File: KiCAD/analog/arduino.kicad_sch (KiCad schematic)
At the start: 49 parts, among them J12 Screw_Terminal_01x04, J13 Screw_Terminal_01x03, J14 Screw_Terminal_01x05, J17 Conn_Coaxial_Small, J18 Conn_Coaxial_Small, J19 Conn_Coaxial_Small, J20 Screw_Terminal_01x04, J21 Screw_Terminal_01x02, J22 Screw_Terminal_01x04, J23 Conn_Coaxial_Small, J24 Conn_Coaxial_Small, J6 Screw_Terminal_01x02, J7 Screw_Terminal_01x02, J8 Screw_Terminal_01x02, J9 Screw_Terminal_01x02, Q4 2N7000, Q5 2N7000, Q6 2N7000, Q7 2N7000, U1 MCP1700x-330xxTO, U17 Adafruit_PCF8575_Breakout, U18 CD14538B, U3 MCP4728

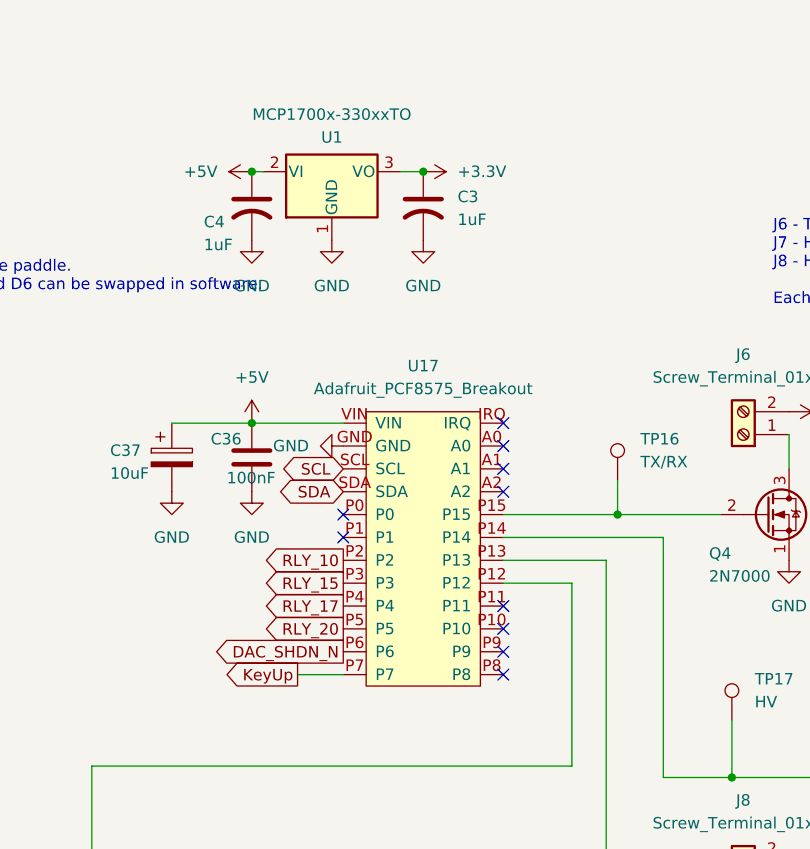
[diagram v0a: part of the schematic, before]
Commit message: KiCad revC: +28V doubler + 5V LDO added to analog/power, ERC clean
- Migrated LT1054 Figure 20 positive doubler from standalone power project
  into analog/power.kicad_sch for the +28V reed-relay rail
- Added LM2940CT-5.0 LDO stage for Metro / Si5351 +5V rail
- analog ERC: 4 messages, all classified as false positives (U9 pin 5
  tied to GND per Fig 20 topology, PCF_P5_SPARE intentionally unused,
  VIN pins now driven by added +5V rail)
- Added QRP Labs 10W PA / 5W PA reference PDFs + 2N7000 + lm2940c
  datasheets to Documentation/QRP_Examples/

Co-Authored-By: Claude Opus 4.7 <noreply@anthropic.com>
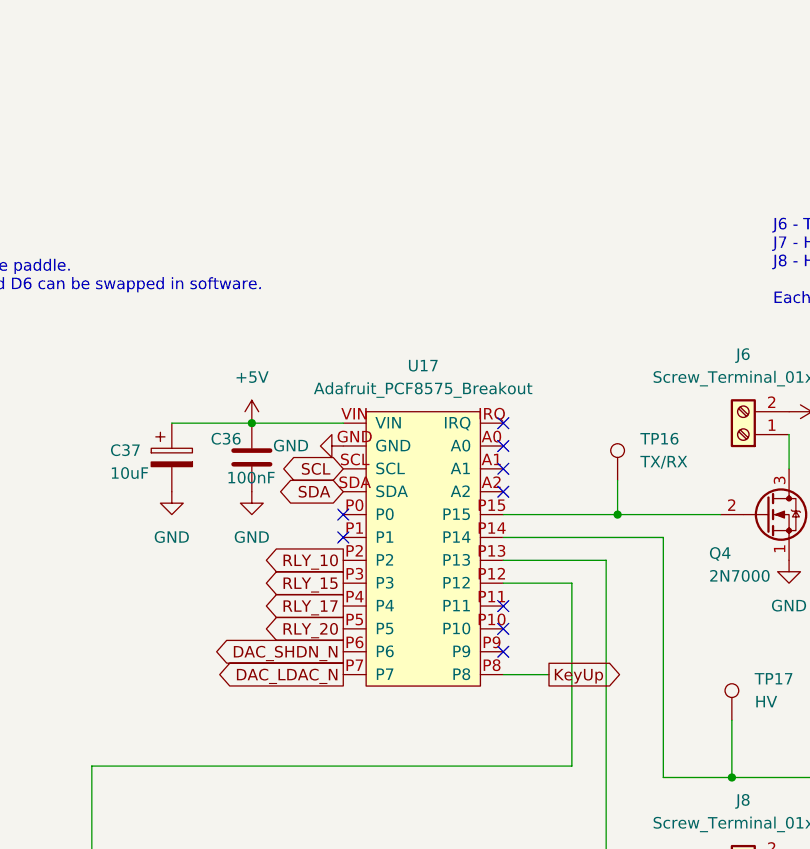
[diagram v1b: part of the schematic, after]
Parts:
- removed C3, C4: 1uF, Capacitor_THT:C_Rect_L7.2mm_W4.5mm_P5.00mm, symbol Device:C_US
- removed U1: MCP1700x-330xxTO, Package_TO_SOT_THT:TO-92_Inline_Wide, symbol Regulator_Linear:MCP1700x-330xxTO
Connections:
- net KeyUp: now also U17.P8; no longer U17.P7
- new net DAC_LDAC_N: U17.P7
- no-connect marks 18 -> 17

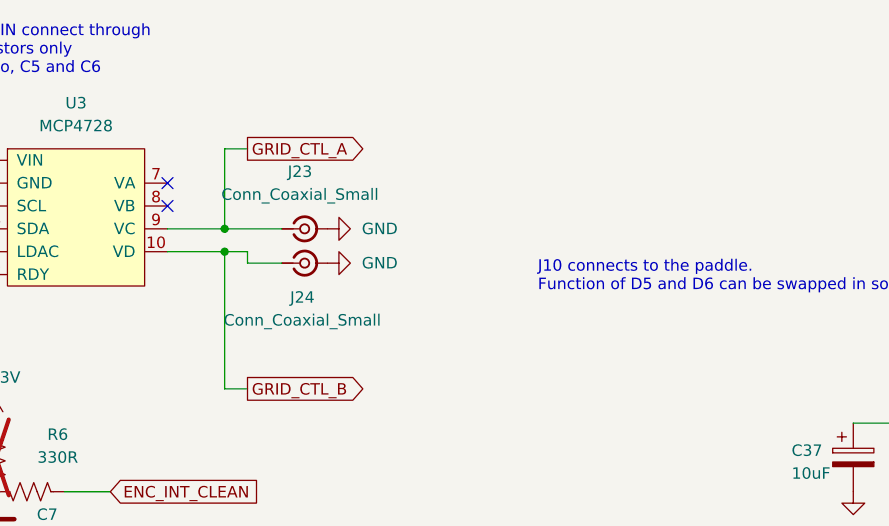
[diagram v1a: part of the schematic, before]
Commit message: KiCad revC: repurpose MCP4728 VA/VB as Bias_A/Bias_B for SS PA
Add Bias_A and Bias_B global labels off the MCP4728 (U? on arduino sheet,
I2C DAC at 0x67) VA and VB outputs. These will route over the umbilical
to the SS PA board to drive IRF510 gate bias — replacing the kit's two
4.7K trimmers with firmware-controlled bias (DAC = 0V during RX).

GRID_CTL_A/B signals preserved on Metro GPIOs but their coax connectors
J23 and J24 marked DNP. Kept in case the shelved tube amp
(driver-less) is revived later.

Co-Authored-By: Claude Opus 4.7 <noreply@anthropic.com>
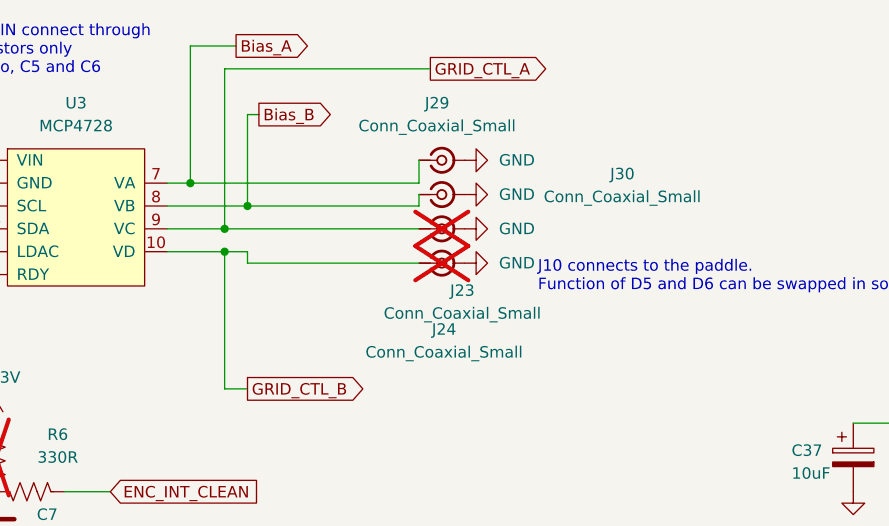
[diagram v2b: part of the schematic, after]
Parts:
- added J29, J30: Conn_Coaxial_Small, xmitter:SMA_Cinch_142-0701-201_Vertical_JackPCB, symbol Connector:Conn_Coaxial_Small
- J23, J24: now not fitted
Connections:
- net GND: now also J29.2 (Ext), J30.2 (Ext)
- net Bias_A: now reaches U3.7 (VA)
- net Bias_A: now also J29.1 (In)
- net Bias_B: now reaches U3.8 (VB)
- net Bias_B: now also J30.1 (In)
- no-connect marks 17 -> 15

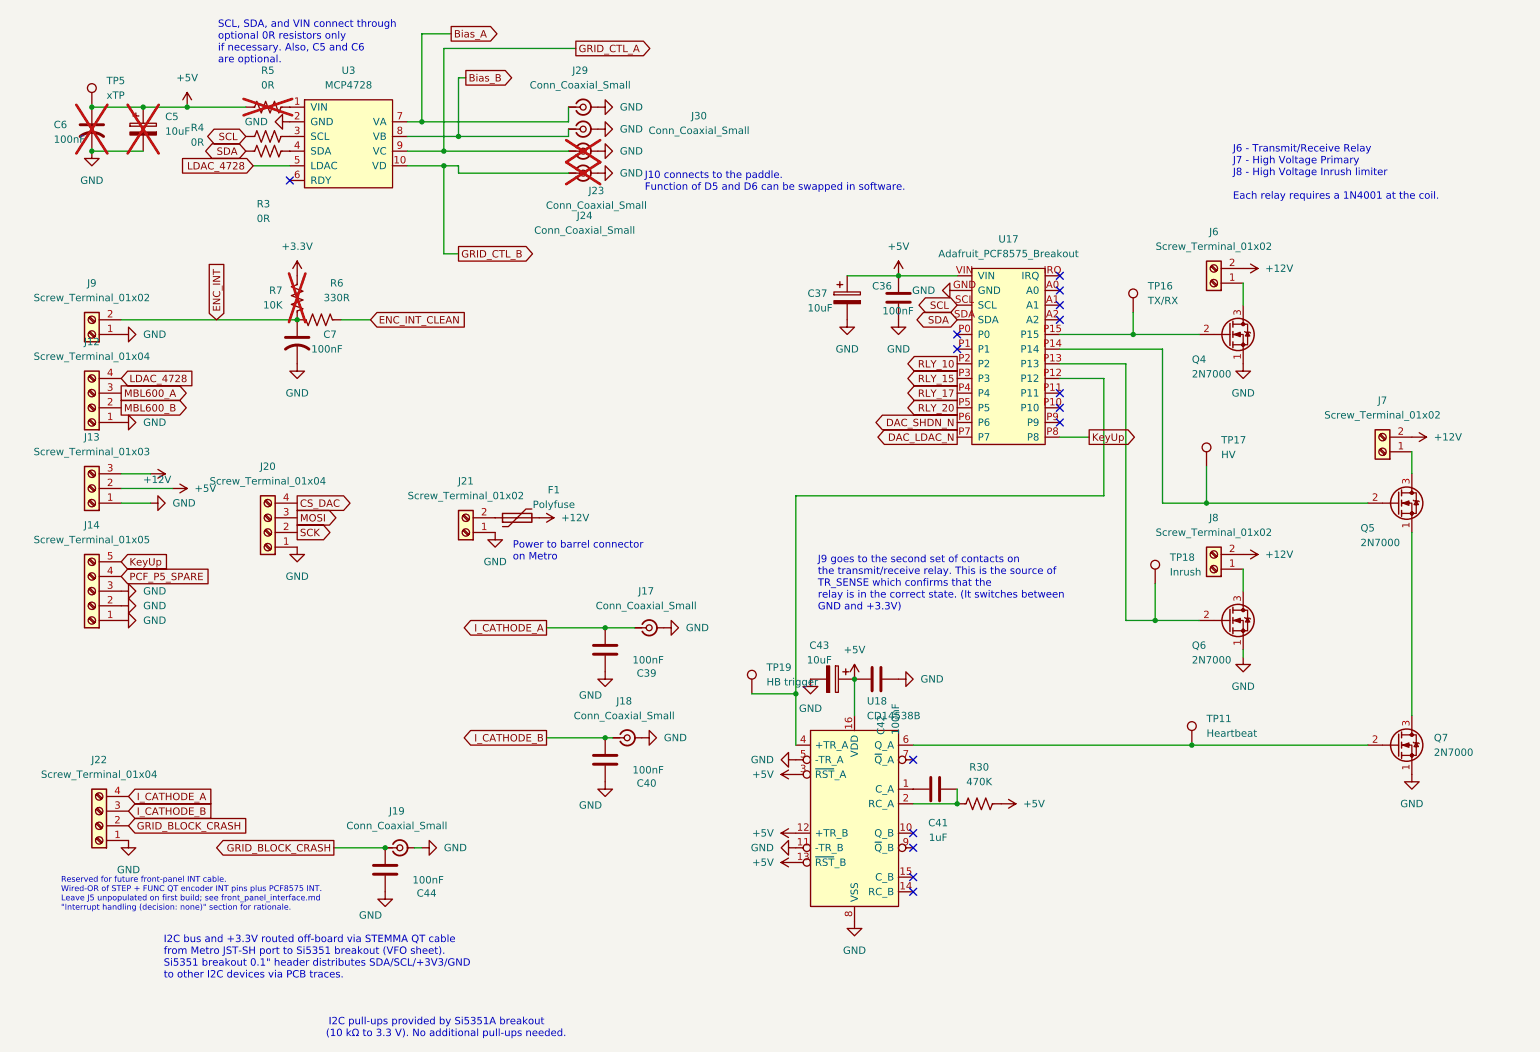
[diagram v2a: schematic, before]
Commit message: KiCad revC: analog arduino sheet — add RJ45 for ss_pa umbilical
Added shielded 8P8C jack on analog board to mate with the ss_pa
board's J7 RJ45. Carries Bias_A_Raw, Bias_B_Raw, +3.3V (power out
to PA board), FAULT_N, Source_Sense_A, Source_Sense_B, plus GND
returns, per the T568B pair assignment pinned in ss_pa.md.

Co-Authored-By: Claude Opus 4.7 <noreply@anthropic.com>
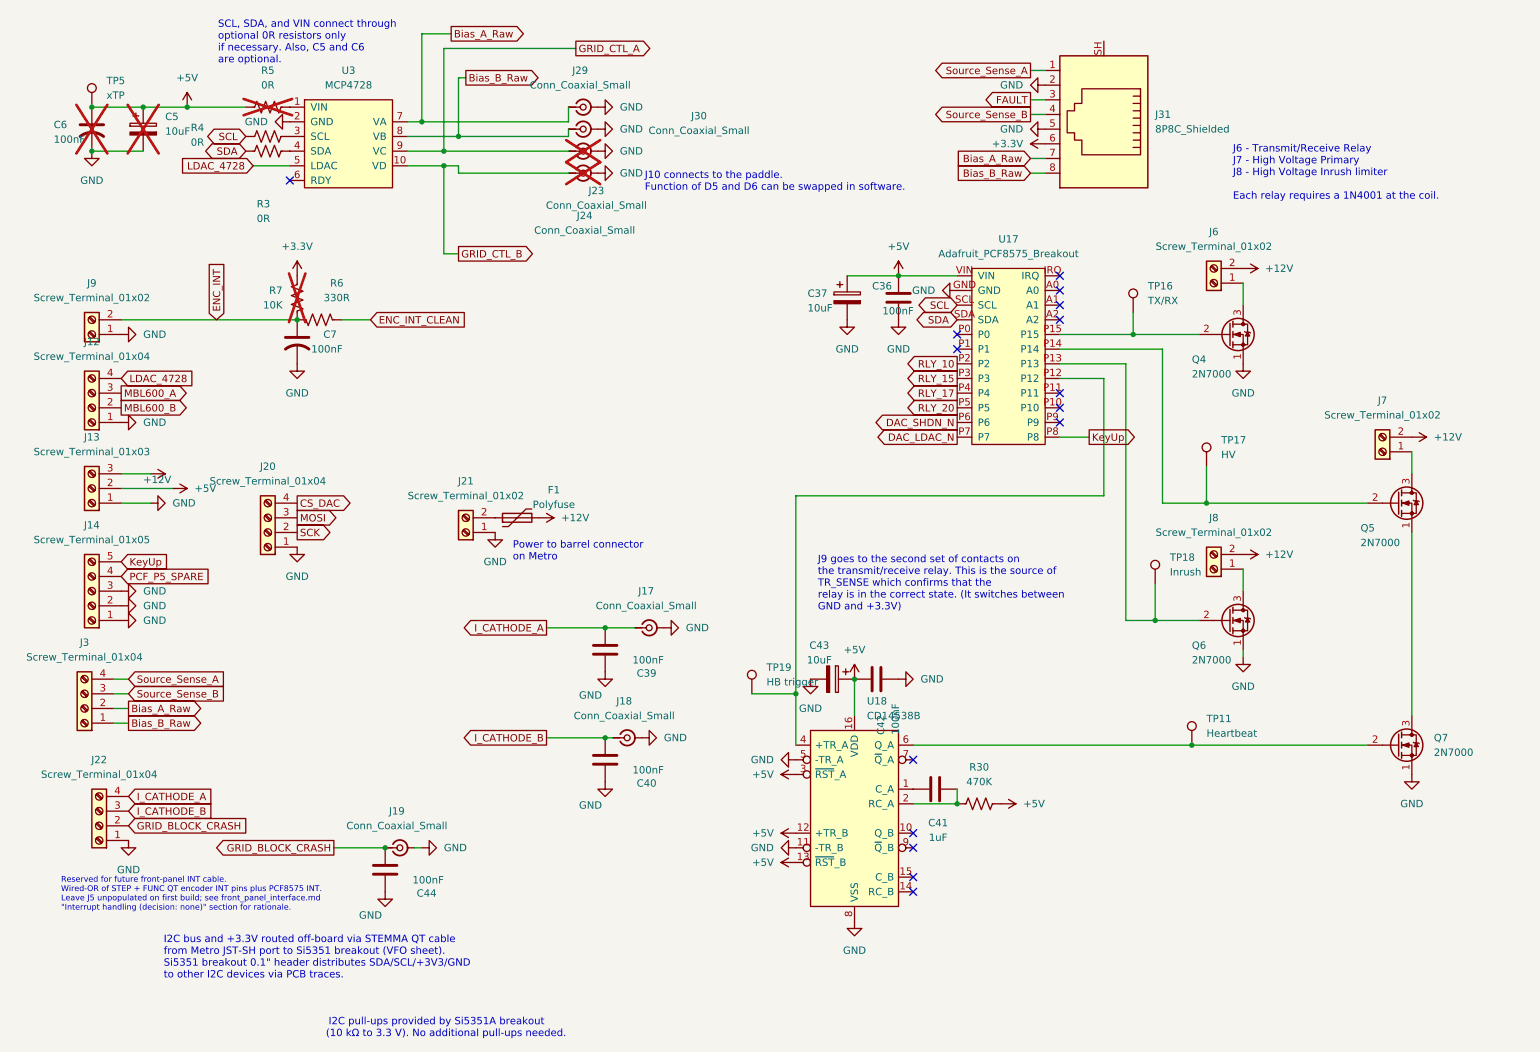
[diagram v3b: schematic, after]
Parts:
- added J3: Screw_Terminal_01x04, symbol Connector:Screw_Terminal_01x04
- added J31: 8P8C_Shielded, xmitter:Amphenol_RJE1D-188_Horizontal_Shielded, symbol Connector:8P8C_Shielded
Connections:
- net +3.3V: now also J31.6
- net GND: now also J31.2, J31.5
- net Bias_A renamed Bias_A_Raw
- net Bias_A_Raw: now also J3.2 (Pin_2), J31.7
- net Bias_B renamed Bias_B_Raw
- net Bias_B_Raw: now also J3.1 (Pin_1), J31.8
- new net FAULT: J31.3
- new net Source_Sense_A: J3.4 (Pin_4), J31.1
- new net Source_Sense_B: J3.3 (Pin_3), J31.4

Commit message: KiCad revC: resolve project-audit findings on analog + protoshield
Fixes the four items from Documentation/2026-10-11-project-audit.md
plus the follow-up Q11 series-R finding:

- Rename FAULT -> FAULT_N on analog arduino and protoshield to match
  ss_pa (active-low per the latest design spec in ss_pa.md)
- Delete the stale PA_OUTPUT_LEVEL global label on dac sheet
  (tube-era signal, no consumer; MCP4922 VoutA now unused and output
  connector marked DNP)
- Fix ENC_INT_CLEAN -> R6 -> ENC_INT signal path on analog arduino
  so the encoder interrupt actually reaches the Metro via protoshield
- Re-export analog.net so it reflects the current schematic (J31
  RJ45 to ss_pa, bias/sense/fault signals, R6 wiring, etc.)

Co-Authored-By: Claude Opus 4.7 <noreply@anthropic.com>
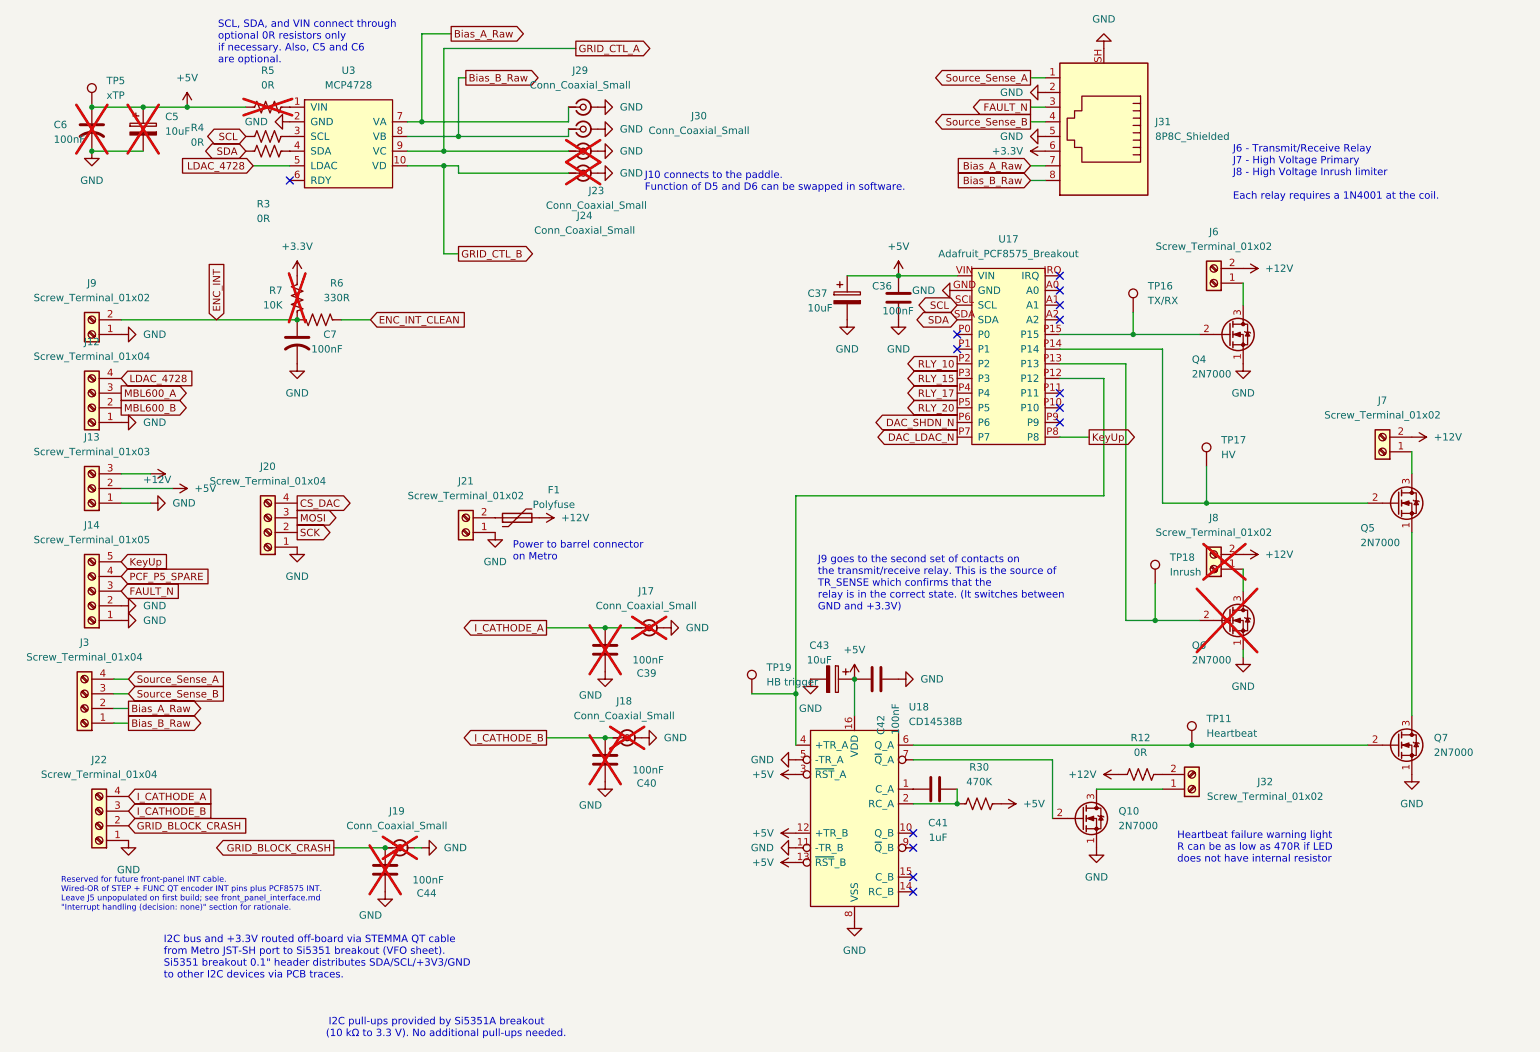
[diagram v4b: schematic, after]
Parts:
- added J32: Screw_Terminal_01x02, symbol Connector:Screw_Terminal_01x02
- added Q10: 2N7000, Package_TO_SOT_THT:TO-92_Inline, symbol Transistor_FET:2N7000
- added R12: 0R, symbol Device:R_US
- C39, C40, C44, J17, J18, J19, J8, Q6: now not fitted
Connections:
- net +12V: now also R12.1
- net GND: now also J31.SH, Q10.1 (S); no longer J14.3 (Pin_3)
- net at U18.7 (~{Q}_A): now also Q10.2 (G)
- net FAULT renamed FAULT_N
- net FAULT_N: now also J14.3 (Pin_3)
- new net: J32.1 (Pin_1), Q10.3 (D)
- new net: J32.2 (Pin_2), R12.2
- no-connect marks 15 -> 14
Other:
- note added: "Heartbeat failure warning light R can be as low as 470R if LED does not have internal resistor"
- moved on the sheet: J31

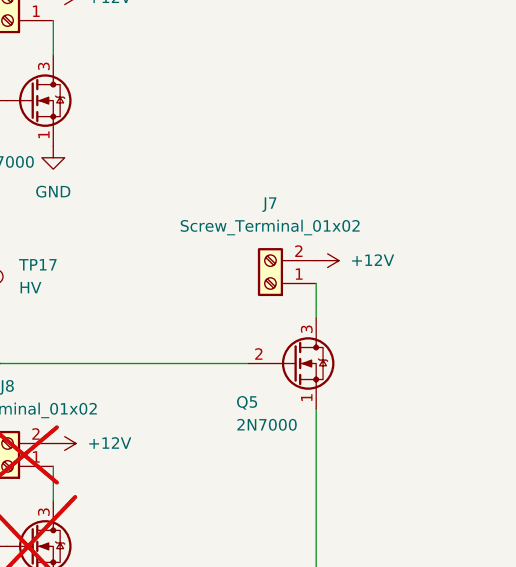
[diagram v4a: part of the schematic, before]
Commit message: KiCad revC: heartbeat-triggered SS PA power disconnect + flyback diodes
analog/power.kicad_sch:
- Added K6 (RLP20-12L10MS2F SPST-NO relay, 10A @ 30V DC contacts,
  12V/20mA coil) in series between +13.8V shack supply and J33
  (new 2-pin screw terminal supplying ss_pa board)
- K6 coil driven by existing Q5+Q7 series safety cascade on
  SS_PWR_RLY net: both Q5 (firmware control via PCF8575 P14) AND
  Q7 (CD14538B heartbeat watchdog Q_A) must be ON for the relay
  to energize. Firmware disable or heartbeat failure cuts PA power.
- Added 90R series resistor in the coil leg to drop +13.8V rail
  down to the 12V coil's nominal operating voltage
- Added D4 (1N4001 flyback diode) across K6 coil, cathode on +13.8V
  side, anode on SS_PWR_RLY (Q5 drain) side
- J7 (tube-era HV primary screw terminal) remains on the SS_PWR_RLY
  net so a future external tube-PA HV relay would share the same
  safety chain

ss_pa/pa_stage.kicad_sch:
- Added D2 (1N5822 Schottky, 3A/40V) flyback diode across L5. When
  the heartbeat relay opens with current flowing through L5, the
  12 uH inductor's stored energy (up to ~13 uJ at 1.5A) would
  otherwise swing the relay-side node hundreds of volts negative
  and arc the K6 contacts. D2 clamps that swing to ~V_f below the
  C6-held +13.8V bus.
- D2 polarity: cathode (pin 1) on J2/relay side, anode (pin 2) on
  +13.8V bus side.

Both netlists re-exported.

Co-Authored-By: Claude Opus 4.7 <noreply@anthropic.com>
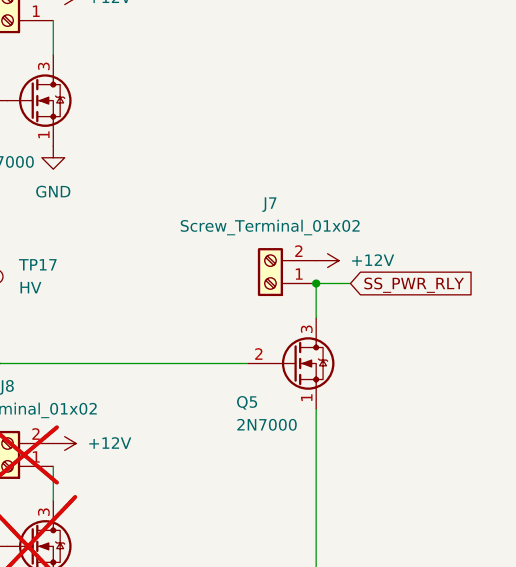
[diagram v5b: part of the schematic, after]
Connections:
- net SS_PWR_RLY: now reaches J7.1 (Pin_1), Q5.3 (D)
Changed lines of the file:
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@@
+	)
+	(junction
+		(at 254 88.9)
+		(diameter 0)
+		(color 0 0 0 0)
 	)
 	(junction
@@
 		(pts
 			(xy 25.4 29.21) (xy 34.29 29.21)
+		)
+		(stroke
+			(width 0)
+			(type default)
+		)
+	)
+	(wire
+		(pts
+			(xy 254 88.9) (xy 257.81 88.9)
 		)
 		(stroke
@@
 			)
 		)
+	)
+	(global_label "SS_PWR_RLY"
+		(shape input)
+		(at 257.81 88.9 0)
+		(fields_autoplaced yes)
+		(effects
+			(font
+				(size 1.27 1.27)
+			)
+			(justify left)
+		)
+		(property "Intersheetrefs" "${INTERSHEET_REFS}"
+			(at 272.5275 88.9 0)
+			(hide yes)
+			(show_name no)
+			(do_not_autoplace no)
+			(effects
+				(font
+					(size 1.27 1.27)
+				)
+				(justify left)
+			)
+		)
